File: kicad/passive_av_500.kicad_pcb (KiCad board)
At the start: 2 copper layers, 57.1 x 29.8 mm, 24 parts, among them J1 Raspberry_Pi_5, J2 Conn_Coaxial, J3 Conn_01x05, J4 AudioJack4

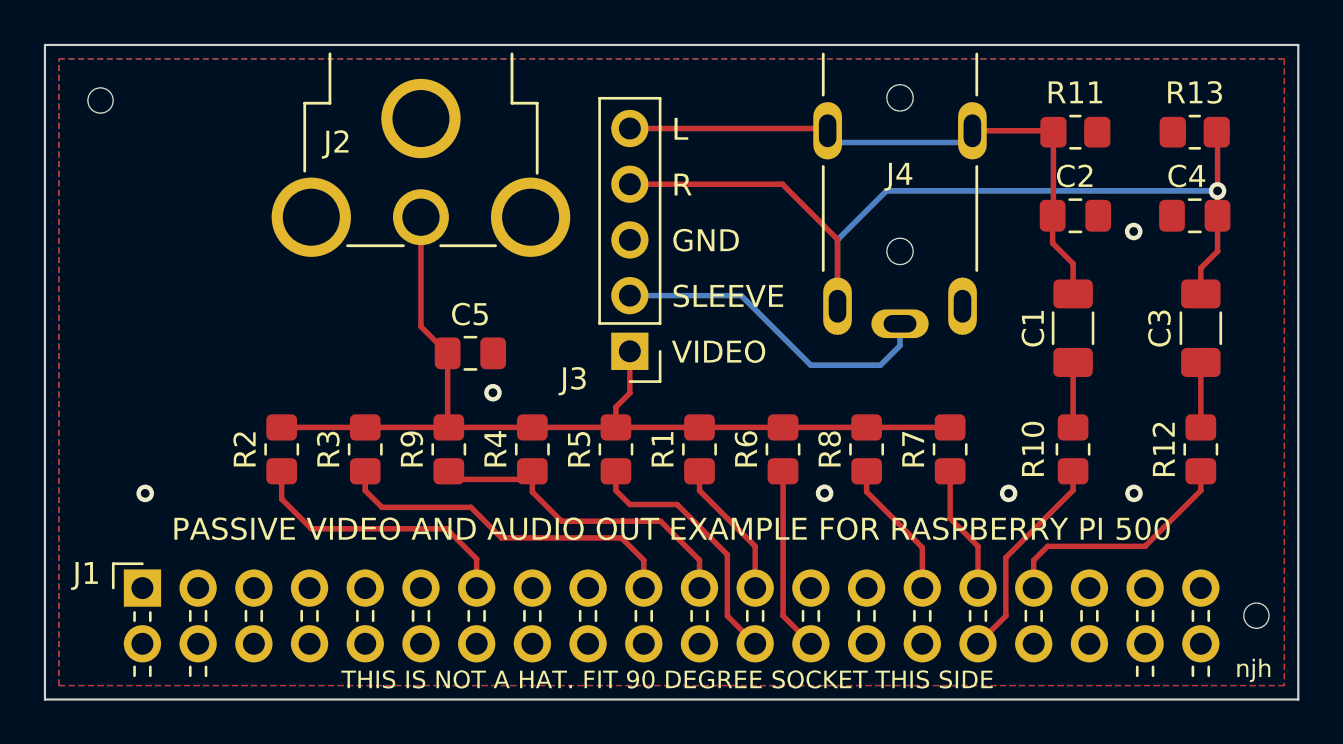
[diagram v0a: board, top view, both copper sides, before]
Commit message: Candidate "rev 2.1" version
Increase R10,R12 and R11,R13 to 300R and 120R. This will slightly
reduce audio level, but ensures peak GPIO current is below 12mA
and total can't exceed 50mA (even if all A/V outputs are shorted).

Update README.md, images and production files.
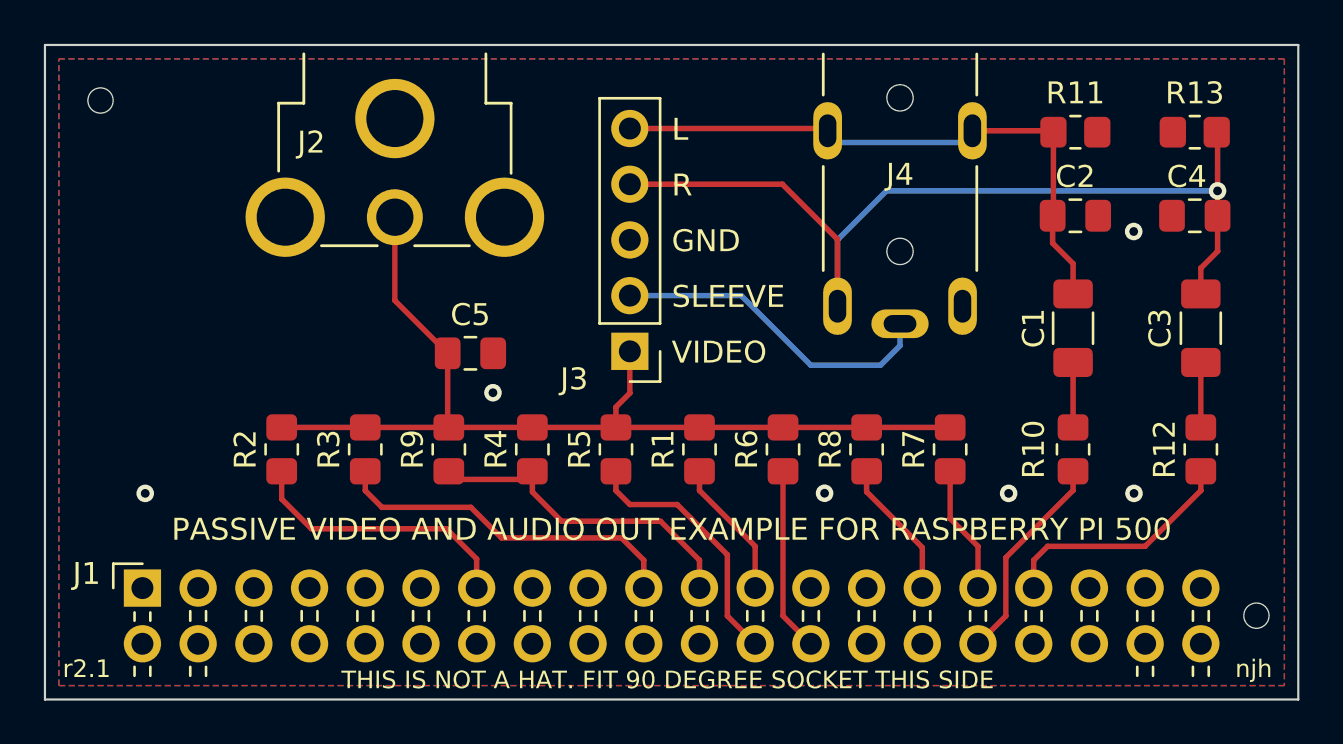
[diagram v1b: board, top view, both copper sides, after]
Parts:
- R10, R12: value 220R -> 300R
- R11, R13: value 100R -> 120R
- moved J2 1.19 mm to (54.1, 29.8)
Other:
- board text added: "r2.1"
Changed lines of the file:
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@@
 	(footprint "misc:CUI_RCJ-014_Inner1Outer2_trimsilk"
 		(layer "F.Cu")
-		(at 55.245 29.845 -90)
+		(at 54.055 29.845 -90)
 		(property "Reference" "J2"
 			(at 2.54 3.81 180)
@@
 			)
 		)
-		(property "Value" "100R"
+		(property "Value" "120R"
 			(at 0 1.65 0)
 			(layer "F.Fab")
@@
 			)
 		)
-		(property "LCSC" "C17408"
+		(property "LCSC" "C17437"
 			(at 0 0 0)
 			(unlocked yes)
@@
 			)
 		)
-		(property "Value" "100R"
+		(property "Value" "120R"
 			(at 0 -1.905 0)
 			(layer "F.Fab")
@@
 			)
 		)
-		(property "LCSC" "C17408"
+		(property "LCSC" "C17437"
 			(at 0 0 180)
 			(unlocked yes)
@@
 			)
 		)
-		(property "Value" "220R"
+		(property "Value" "300R"
 			(at 0 1.65 90)
 			(layer "F.Fab")
@@
 			)
 		)
-		(property "LCSC" "C17557"
+		(property "LCSC" "C17617"
 			(at 0 0 90)
 			(unlocked yes)
@@
 			)
 		)
-		(property "Value" "220R"
+		(property "Value" "300R"
 			(at 0 1.65 90)
 			(layer "F.Fab")
@@
 			)
 		)
-		(property "LCSC" "C17557"
+		(property "LCSC" "C17617"
 			(at 0 0 90)
 			(unlocked yes)
@@
 		)
 	)
+	(gr_text "r2.1"
+		(at 40.005 56.388 0)
+		(layer "F.SilkS")
+		(effects
+			(font
+				(size 0.8 0.8)
+				(thickness 0.1)
+			)
+		)
+	)
 	(gr_text "PASSIVE VIDEO AND AUDIO OUT EXAMPLE FOR RASPBERRY PI 500"
 		(at 66.675 50.038 0)
@@
 	)
 	(segment
-		(start 55.245 40.7825)
-		(end 55.245 35.795)
-		(width 0.25)
-		(layer "F.Cu")
-		(net 39)
-	)
-	(segment
 		(start 67.945 45.38)
 		(end 64.135 45.38)
@@
 	(segment
 		(start 56.4625 42)
+		(end 54.055 39.5925)
+		(width 0.25)
+		(layer "F.Cu")
+		(net 39)
+	)
+	(segment
+		(start 54.055 39.5925)
+		(end 54.055 35.795)
+		(width 0.25)
+		(layer "F.Cu")
+		(net 39)
+	)
+	(segment
+		(start 56.4625 42)
 		(end 56.4625 45.3275)
 		(width 0.25)
@@
 		(width 0.25)
 		(layer "F.Cu")
-		(net 39)
-	)
-	(segment
-		(start 56.4625 42)
-		(end 55.245 40.7825)
-		(width 0.25)
-		(layer "F.Cu")
